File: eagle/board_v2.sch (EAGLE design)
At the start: 34 parts, among them J1 RJ11-4X, Q1 BD140, Q10 BD140, Q11 BD140, Q12 BD140, Q13 BD140, Q14 BD140, Q15 BD140, Q2 BD140, Q3 BD140, Q4 BD140, Q5 BD140, Q6 BD140, Q7 BD140, Q8 BD140, Q9 BD140, X1 RJ45-8X, X2 RJ45-8X, X3 RJ45-8X, X4 RJ45-8X, X5 RJ45-8X

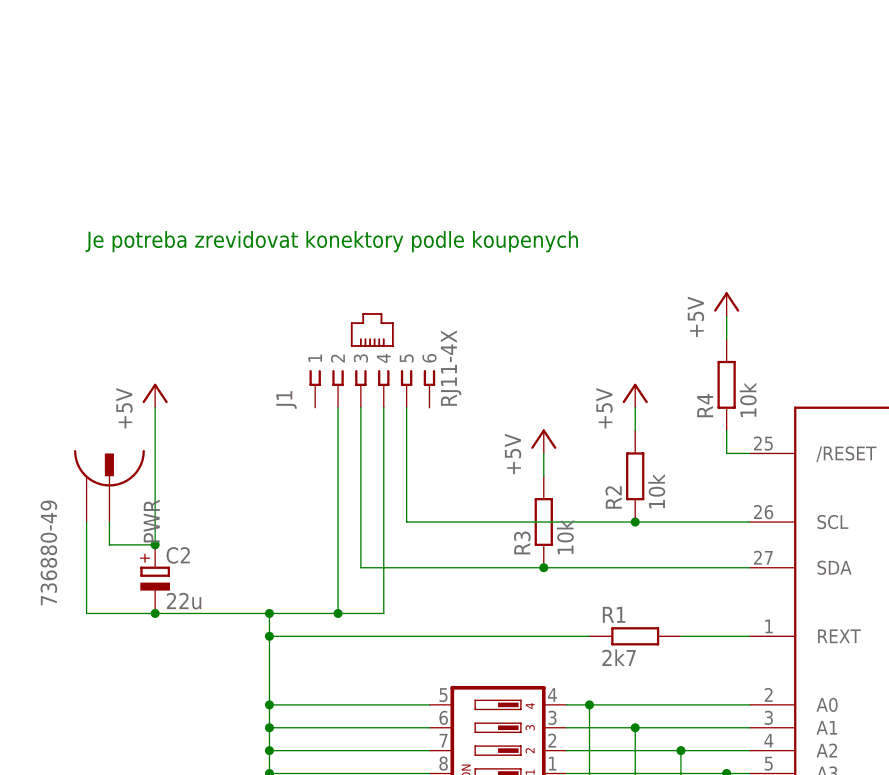
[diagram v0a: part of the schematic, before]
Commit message: board chaining connectors
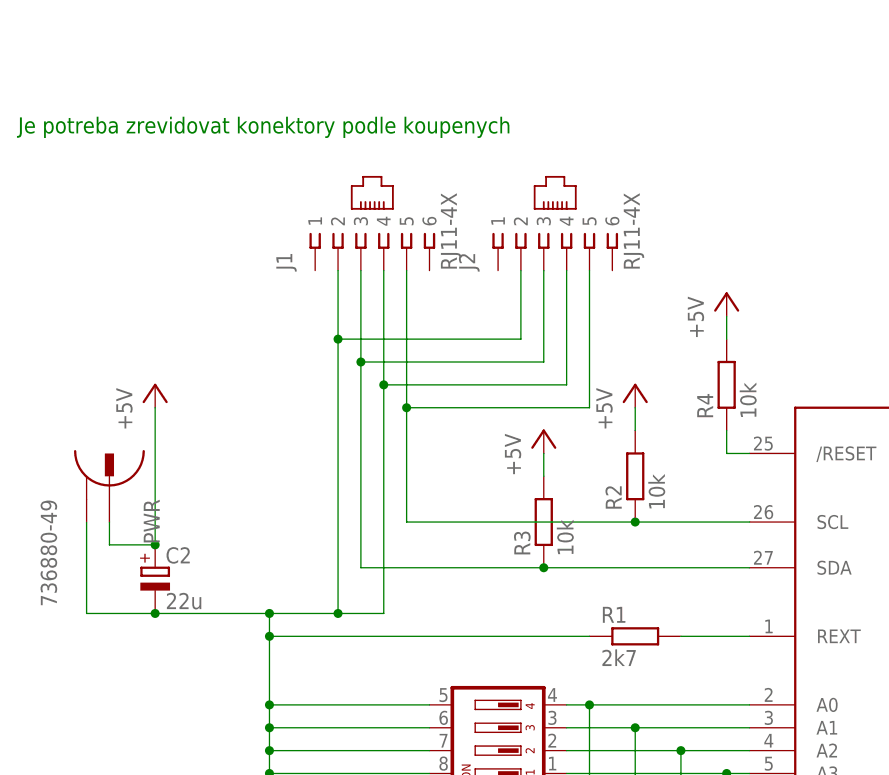
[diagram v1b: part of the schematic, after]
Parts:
- added J2: RJ11-4X, con-tycoelectronics:RJ11-4X
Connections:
- net GND: now also J2.2, J2.4
- net N$37: now also J2.5
- net N$38: now also J2.3
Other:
- moved on the sheet: J1
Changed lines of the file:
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@@
 <setting verticaltext="up"/>
 </settings>
-<grid distance="2.54" unitdist="mm" unit="mm" style="lines" multiple="1" display="yes" altdistance="0.254" altunitdist="mm" altunit="mm"/>
+<grid distance="0.1" unitdist="inch" unit="inch" style="lines" multiple="1" display="no" altdistance="0.01" altunitdist="inch" altunit="inch"/>
 <layers>
 <layer number="1" name="Top" color="4" fill="1" visible="no" active="no"/>
@@
 </part>
 <part name="J1" library="con-tycoelectronics" deviceset="RJ11" device="" technology="-4X"/>
+<part name="J2" library="con-tycoelectronics" deviceset="RJ11" device="" technology="-4X">
+<attribute name="MF" value=""/>
+<attribute name="MPN" value="6609214-3"/>
+<attribute name="OC_FARNELL" value="unknown"/>
+<attribute name="OC_NEWARK" value="19R7022"/>
+</part>
 </parts>
 <sheets>
 <sheet>
 <plain>
-<text x="-50.8" y="104.14" size="1.778" layer="91">Je potreba zrevidovat konektory podle koupenych</text>
+<text x="-58.42" y="116.84" size="1.778" layer="91">Je potreba zrevidovat konektory podle koupenych</text>
 </plain>
 <instances>
@@
 <instance part="P+11" gate="1" x="27.94" y="15.24" rot="R270"/>
 <instance part="S1" gate="A" x="-5.08" y="48.26" rot="R90"/>
-<instance part="J1" gate="G$1" x="-20.32" y="88.9" rot="R90"/>
+<instance part="J1" gate="G$1" x="-20.32" y="104.14" rot="R90"/>
+<instance part="J2" gate="G$1" x="0" y="104.14" rot="R90"/>
 </instances>
 <busses>
@@
 <junction x="-30.48" y="60.96"/>
 <pinref part="J1" gate="G$1" pin="4"/>
-<wire x1="-17.78" y1="63.5" x2="-17.78" y2="86.36" width="0.1524" layer="91"/>
+<wire x1="-17.78" y1="63.5" x2="-17.78" y2="88.9" width="0.1524" layer="91"/>
 <pinref part="J1" gate="G$1" pin="2"/>
-<wire x1="-22.86" y1="86.36" x2="-22.86" y2="63.5" width="0.1524" layer="91"/>
+<wire x1="-17.78" y1="88.9" x2="-17.78" y2="101.6" width="0.1524" layer="91"/>
+<wire x1="-22.86" y1="101.6" x2="-22.86" y2="93.98" width="0.1524" layer="91"/>
 <junction x="-22.86" y="63.5"/>
+<pinref part="J2" gate="G$1" pin="4"/>
+<wire x1="-22.86" y1="93.98" x2="-22.86" y2="63.5" width="0.1524" layer="91"/>
+<wire x1="2.54" y1="101.6" x2="2.54" y2="88.9" width="0.1524" layer="91"/>
+<wire x1="2.54" y1="88.9" x2="-17.78" y2="88.9" width="0.1524" layer="91"/>
+<pinref part="J2" gate="G$1" pin="2"/>
+<wire x1="-2.54" y1="101.6" x2="-2.54" y2="93.98" width="0.1524" layer="91"/>
+<wire x1="-2.54" y1="93.98" x2="-22.86" y2="93.98" width="0.1524" layer="91"/>
+<junction x="-17.78" y="88.9"/>
+<junction x="-22.86" y="93.98"/>
 </segment>
 <segment>
@@
 <pinref part="J1" gate="G$1" pin="5"/>
 <wire x1="-15.24" y1="73.66" x2="-15.24" y2="86.36" width="0.1524" layer="91"/>
+<pinref part="J2" gate="G$1" pin="5"/>
+<wire x1="-15.24" y1="86.36" x2="-15.24" y2="101.6" width="0.1524" layer="91"/>
+<wire x1="5.08" y1="101.6" x2="5.08" y2="86.36" width="0.1524" layer="91"/>
+<wire x1="5.08" y1="86.36" x2="-15.24" y2="86.36" width="0.1524" layer="91"/>
+<junction x="-15.24" y="86.36"/>
 </segment>
 </net>
@@
 <wire x1="22.86" y1="68.58" x2="0" y2="68.58" width="0.1524" layer="91"/>
 <pinref part="J1" gate="G$1" pin="3"/>
-<wire x1="-20.32" y1="86.36" x2="-20.32" y2="68.58" width="0.1524" layer="91"/>
+<wire x1="-20.32" y1="101.6" x2="-20.32" y2="91.44" width="0.1524" layer="91"/>
+<wire x1="-20.32" y1="91.44" x2="-20.32" y2="68.58" width="0.1524" layer="91"/>
 <wire x1="-20.32" y1="68.58" x2="0" y2="68.58" width="0.1524" layer="91"/>
 <junction x="0" y="68.58"/>
-</segment>
-</net>
+<pinref part="J2" gate="G$1" pin="3"/>
+<wire x1="0" y1="101.6" x2="0" y2="91.44" width="0.1524" layer="91"/>
+<wire x1="0" y1="91.44" x2="-20.32" y2="91.44" width="0.1524" layer="91"/>
+<junction x="-20.32" y="91.44"/>
+</segment>
+</net>

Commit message: cinch -> svorkovnice
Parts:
- removed PWR: 736880-49, con-conrad:736880-49
- added GND, VCC: WIREPAD3,17/1,3, wirepad:WIREPAD3,17/1,3
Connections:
- net +5V: now also VCC.P; no longer PWR.1
- net GND: now also GND.P; no longer PWR.2
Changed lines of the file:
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@@
 <part name="U$1" library="tlc" deviceset="TLC59116" device=""/>
 <part name="GND9" library="supply1" deviceset="GND" device=""/>
-<part name="PWR" library="con-conrad" deviceset="736880-49" device=""/>
 <part name="P+7" library="supply1" deviceset="+5V" device=""/>
 <part name="P+8" library="supply1" deviceset="+5V" device=""/>
@@
 <attribute name="OC_NEWARK" value="19R7022"/>
 </part>
+<part name="GND" library="wirepad" deviceset="WIREPAD" device="3,17/1,3"/>
+<part name="VCC" library="wirepad" deviceset="WIREPAD" device="3,17/1,3"/>
 </parts>
 <sheets>
@@
 <instance part="U$1" gate="G$1" x="48.26" y="63.5"/>
 <instance part="GND9" gate="1" x="-30.48" y="40.64"/>
-<instance part="PWR" gate="G$1" x="-48.26" y="76.2" rot="R270"/>
 <instance part="P+7" gate="1" x="10.16" y="88.9"/>
 <instance part="P+8" gate="1" x="0" y="83.82"/>
@@
 <instance part="J1" gate="G$1" x="-20.32" y="104.14" rot="R90"/>
 <instance part="J2" gate="G$1" x="0" y="104.14" rot="R90"/>
+<instance part="GND" gate="G$1" x="-68.58" y="91.44" rot="R270"/>
+<instance part="VCC" gate="G$1" x="-58.42" y="91.44" rot="R270"/>
 </instances>
 <busses>
@@
 <pinref part="C2" gate="G$1" pin="+"/>
 <wire x1="-43.18" y1="86.36" x2="-43.18" y2="71.12" width="0.1524" layer="91"/>
-<pinref part="PWR" gate="G$1" pin="1"/>
-<wire x1="-48.26" y1="73.66" x2="-48.26" y2="71.12" width="0.1524" layer="91"/>
-<wire x1="-43.18" y1="71.12" x2="-48.26" y2="71.12" width="0.1524" layer="91"/>
 <junction x="-43.18" y="71.12"/>
+<pinref part="VCC" gate="G$1" pin="P"/>
+<wire x1="-43.18" y1="71.12" x2="-58.42" y2="71.12" width="0.1524" layer="91"/>
+<wire x1="-58.42" y1="71.12" x2="-58.42" y2="88.9" width="0.1524" layer="91"/>
 </segment>
 <segment>
@@
 <pinref part="S1" gate="A" pin="7"/>
 <pinref part="S1" gate="A" pin="8"/>
-<pinref part="PWR" gate="G$1" pin="2"/>
-<wire x1="-50.8" y1="73.66" x2="-50.8" y2="63.5" width="0.1524" layer="91"/>
-<wire x1="-50.8" y1="63.5" x2="-43.18" y2="63.5" width="0.1524" layer="91"/>
+<wire x1="-68.58" y1="88.9" x2="-68.58" y2="63.5" width="0.1524" layer="91"/>
+<wire x1="-68.58" y1="63.5" x2="-43.18" y2="63.5" width="0.1524" layer="91"/>
 <wire x1="-43.18" y1="63.5" x2="-30.48" y2="63.5" width="0.1524" layer="91"/>
 <wire x1="-30.48" y1="63.5" x2="-22.86" y2="63.5" width="0.1524" layer="91"/>
@@
 <junction x="-17.78" y="88.9"/>
 <junction x="-22.86" y="93.98"/>
-</segment>
-<segment>
+<pinref part="GND" gate="G$1" pin="P"/>
+</segment>
+<segment>

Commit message: moar changes
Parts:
- removed GND, VCC: WIREPAD3,17/1,3, wirepad:WIREPAD3,17/1,3
- added X6: RJ45-8X, con-tycoelectronics:RJ45-8X
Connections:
- net +5V: now also X6.1, X6.2, X6.3, X6.4; no longer VCC.P
- net GND: now also X6.5, X6.6, X6.7, X6.8; no longer GND.P
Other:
- note removed: "Je potreba zrevidovat konektory podle koupenych"
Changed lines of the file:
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@@
 <attribute name="OC_NEWARK" value="19R7022"/>
 </part>
-<part name="GND" library="wirepad" deviceset="WIREPAD" device="3,17/1,3"/>
-<part name="VCC" library="wirepad" deviceset="WIREPAD" device="3,17/1,3"/>
+<part name="X6" library="con-tycoelectronics" deviceset="RJ45" device="" technology="-8X"/>
 </parts>
 <sheets>
 <sheet>
 <plain>
-<text x="-58.42" y="116.84" size="1.778" layer="91">Je potreba zrevidovat konektory podle koupenych</text>
 </plain>
 <instances>
@@
 <instance part="J1" gate="G$1" x="-20.32" y="104.14" rot="R90"/>
 <instance part="J2" gate="G$1" x="0" y="104.14" rot="R90"/>
-<instance part="GND" gate="G$1" x="-68.58" y="91.44" rot="R270"/>
-<instance part="VCC" gate="G$1" x="-58.42" y="91.44" rot="R270"/>
+<instance part="X6" gate="G$1" x="-63.5" y="106.68" rot="MR90"/>
 </instances>
 <busses>
@@
 <wire x1="-43.18" y1="86.36" x2="-43.18" y2="71.12" width="0.1524" layer="91"/>
 <junction x="-43.18" y="71.12"/>
-<pinref part="VCC" gate="G$1" pin="P"/>
 <wire x1="-43.18" y1="71.12" x2="-58.42" y2="71.12" width="0.1524" layer="91"/>
-<wire x1="-58.42" y1="71.12" x2="-58.42" y2="88.9" width="0.1524" layer="91"/>
+<wire x1="-58.42" y1="71.12" x2="-58.42" y2="101.6" width="0.1524" layer="91"/>
+<wire x1="-58.42" y1="101.6" x2="-55.88" y2="101.6" width="0.1524" layer="91"/>
+<pinref part="X6" gate="G$1" pin="1"/>
+<wire x1="-55.88" y1="101.6" x2="-55.88" y2="104.14" width="0.1524" layer="91"/>
+<pinref part="X6" gate="G$1" pin="2"/>
+<wire x1="-58.42" y1="101.6" x2="-58.42" y2="104.14" width="0.1524" layer="91"/>
+<pinref part="X6" gate="G$1" pin="3"/>
+<wire x1="-58.42" y1="101.6" x2="-60.96" y2="101.6" width="0.1524" layer="91"/>
+<wire x1="-60.96" y1="101.6" x2="-60.96" y2="104.14" width="0.1524" layer="91"/>
+<pinref part="X6" gate="G$1" pin="4"/>
+<wire x1="-60.96" y1="101.6" x2="-63.5" y2="101.6" width="0.1524" layer="91"/>
+<wire x1="-63.5" y1="101.6" x2="-63.5" y2="104.14" width="0.1524" layer="91"/>
+<junction x="-58.42" y="101.6"/>
 </segment>
 <segment>
@@
 <pinref part="S1" gate="A" pin="7"/>
 <pinref part="S1" gate="A" pin="8"/>
-<wire x1="-68.58" y1="88.9" x2="-68.58" y2="63.5" width="0.1524" layer="91"/>
+<wire x1="-68.58" y1="104.14" x2="-68.58" y2="101.6" width="0.1524" layer="91"/>
+<wire x1="-68.58" y1="101.6" x2="-68.58" y2="63.5" width="0.1524" layer="91"/>
 <wire x1="-68.58" y1="63.5" x2="-43.18" y2="63.5" width="0.1524" layer="91"/>
 <wire x1="-43.18" y1="63.5" x2="-30.48" y2="63.5" width="0.1524" layer="91"/>
@@
 <junction x="-17.78" y="88.9"/>
 <junction x="-22.86" y="93.98"/>
-<pinref part="GND" gate="G$1" pin="P"/>
-</segment>
-<segment>
+<pinref part="X6" gate="G$1" pin="6"/>
+<pinref part="X6" gate="G$1" pin="8"/>
+<wire x1="-68.58" y1="101.6" x2="-71.12" y2="101.6" width="0.1524" layer="91"/>
+<wire x1="-71.12" y1="101.6" x2="-73.66" y2="101.6" width="0.1524" layer="91"/>
+<wire x1="-73.66" y1="101.6" x2="-73.66" y2="104.14" width="0.1524" layer="91"/>
+<pinref part="X6" gate="G$1" pin="7"/>
+<wire x1="-71.12" y1="101.6" x2="-71.12" y2="104.14" width="0.1524" layer="91"/>
+<pinref part="X6" gate="G$1" pin="5"/>
+<wire x1="-68.58" y1="101.6" x2="-66.04" y2="101.6" width="0.1524" layer="91"/>
+<wire x1="-66.04" y1="101.6" x2="-66.04" y2="104.14" width="0.1524" layer="91"/>
+<junction x="-68.58" y="101.6"/>
+</segment>
+<segment>

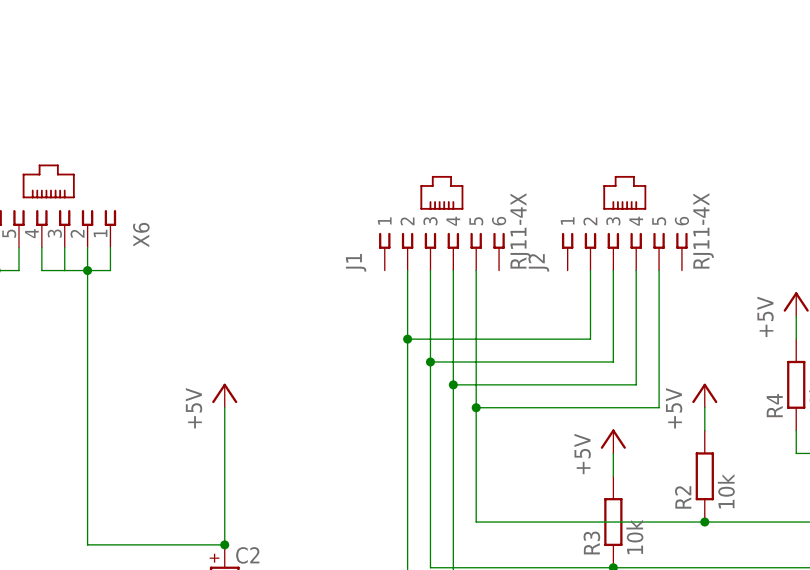
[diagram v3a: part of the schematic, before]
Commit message: i2c in crossover; removed jumper wires
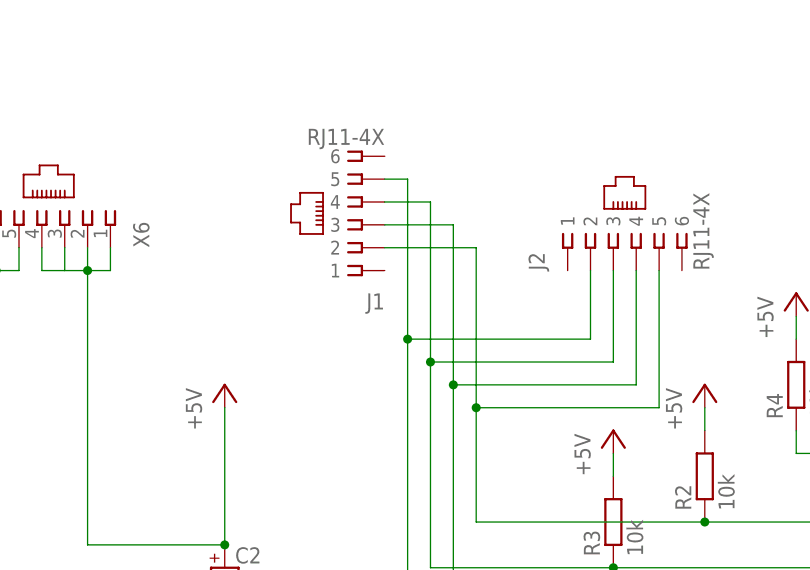
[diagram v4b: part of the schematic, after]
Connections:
- net GND: now also J1.3, J1.5; no longer J1.2, J1.4
- net N$37: now also J1.2; no longer J1.5
- net N$38: now also J1.4; no longer J1.3
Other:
- moved on the sheet: J1
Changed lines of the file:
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@@
 <instance part="P+11" gate="1" x="27.94" y="15.24" rot="R270"/>
 <instance part="S1" gate="A" x="-5.08" y="48.26" rot="R90"/>
-<instance part="J1" gate="G$1" x="-20.32" y="104.14" rot="R90"/>
+<instance part="J1" gate="G$1" x="-27.94" y="106.68" rot="R180"/>
 <instance part="J2" gate="G$1" x="0" y="104.14" rot="R90"/>
 <instance part="X6" gate="G$1" x="-63.5" y="106.68" rot="MR90"/>
@@
 <junction x="-30.48" y="63.5"/>
 <junction x="-30.48" y="60.96"/>
-<pinref part="J1" gate="G$1" pin="4"/>
 <wire x1="-17.78" y1="63.5" x2="-17.78" y2="88.9" width="0.1524" layer="91"/>
-<pinref part="J1" gate="G$1" pin="2"/>
-<wire x1="-17.78" y1="88.9" x2="-17.78" y2="101.6" width="0.1524" layer="91"/>
-<wire x1="-22.86" y1="101.6" x2="-22.86" y2="93.98" width="0.1524" layer="91"/>
 <junction x="-22.86" y="63.5"/>
 <pinref part="J2" gate="G$1" pin="4"/>
@@
 <wire x1="-2.54" y1="101.6" x2="-2.54" y2="93.98" width="0.1524" layer="91"/>
 <wire x1="-2.54" y1="93.98" x2="-22.86" y2="93.98" width="0.1524" layer="91"/>
-<junction x="-17.78" y="88.9"/>
-<junction x="-22.86" y="93.98"/>
 <pinref part="X6" gate="G$1" pin="6"/>
 <pinref part="X6" gate="G$1" pin="8"/>
@@
 <wire x1="-66.04" y1="101.6" x2="-66.04" y2="104.14" width="0.1524" layer="91"/>
 <junction x="-68.58" y="101.6"/>
+<pinref part="J1" gate="G$1" pin="3"/>
+<wire x1="-25.4" y1="106.68" x2="-17.78" y2="106.68" width="0.1524" layer="91"/>
+<wire x1="-17.78" y1="106.68" x2="-17.78" y2="88.9" width="0.1524" layer="91"/>
+<pinref part="J1" gate="G$1" pin="5"/>
+<wire x1="-25.4" y1="111.76" x2="-22.86" y2="111.76" width="0.1524" layer="91"/>
+<wire x1="-22.86" y1="111.76" x2="-22.86" y2="93.98" width="0.1524" layer="91"/>
+<junction x="-22.86" y="93.98"/>
+<junction x="-17.78" y="88.9"/>
 </segment>
 <segment>
@@
 <wire x1="10.16" y1="73.66" x2="-15.24" y2="73.66" width="0.1524" layer="91"/>
 <junction x="10.16" y="73.66"/>
-<pinref part="J1" gate="G$1" pin="5"/>
 <wire x1="-15.24" y1="73.66" x2="-15.24" y2="86.36" width="0.1524" layer="91"/>
 <pinref part="J2" gate="G$1" pin="5"/>
-<wire x1="-15.24" y1="86.36" x2="-15.24" y2="101.6" width="0.1524" layer="91"/>
 <wire x1="5.08" y1="101.6" x2="5.08" y2="86.36" width="0.1524" layer="91"/>
 <wire x1="5.08" y1="86.36" x2="-15.24" y2="86.36" width="0.1524" layer="91"/>
+<pinref part="J1" gate="G$1" pin="2"/>
+<wire x1="-25.4" y1="104.14" x2="-15.24" y2="104.14" width="0.1524" layer="91"/>
+<wire x1="-15.24" y1="104.14" x2="-15.24" y2="86.36" width="0.1524" layer="91"/>
 <junction x="-15.24" y="86.36"/>
 </segment>
@@
 <pinref part="R3" gate="G$1" pin="1"/>
 <wire x1="22.86" y1="68.58" x2="0" y2="68.58" width="0.1524" layer="91"/>
-<pinref part="J1" gate="G$1" pin="3"/>
-<wire x1="-20.32" y1="101.6" x2="-20.32" y2="91.44" width="0.1524" layer="91"/>
 <wire x1="-20.32" y1="91.44" x2="-20.32" y2="68.58" width="0.1524" layer="91"/>
 <wire x1="-20.32" y1="68.58" x2="0" y2="68.58" width="0.1524" layer="91"/>
@@
 <wire x1="0" y1="101.6" x2="0" y2="91.44" width="0.1524" layer="91"/>
 <wire x1="0" y1="91.44" x2="-20.32" y2="91.44" width="0.1524" layer="91"/>
+<pinref part="J1" gate="G$1" pin="4"/>
+<wire x1="-25.4" y1="109.22" x2="-20.32" y2="109.22" width="0.1524" layer="91"/>
+<wire x1="-20.32" y1="109.22" x2="-20.32" y2="91.44" width="0.1524" layer="91"/>
 <junction x="-20.32" y="91.44"/>
 </segment>

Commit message: board v2.2
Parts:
- removed S1: (no value), switch-dil:DS04
- removed X1, X2, X3, X4, X5: RJ45-8X, con-tycoelectronics:RJ45-8X
- added C3: 1u, resistor:C-EUC1206
- added JP1: (no value), pinhead:PINHD-2X4
- added PWR: ARK210/2EX, con-brm:ARK210/2EX
- added X10, X7, X8, X9: 22-23-2041, con-molex:22-23-2041
- C2: device resistor:CPOL-EUC -> resistor:CPOL-EUE2.5-5
- R4: value 10k -> 4k7
- X6: value RJ45-8X -> 22-23-2041; device con-tycoelectronics:RJ45-8X -> con-molex:22-23-2041
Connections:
- net +5V: now also C3.1, PWR.1, X10-2.S, X6-2.S, X7-2.S, X8-2.S, X9-2.S; no longer X1.4, X2.4, X3.4, X4.4, X5.4, X6.1, X6.2, X6.3, X6.4
- net GND: now also C3.2, JP1.1, JP1.3, JP1.5, JP1.7, PWR.2; no longer S1.5, S1.6, S1.7, S1.8, X6.5, X6.6, X6.7, X6.8
- net N$1: now also X6-1.S; no longer X1.2
- net N$10: now also X10-1.S; no longer X4.2
- net N$11: now also X10-3.S; no longer X4.6
- net N$12: now also X10-4.S; no longer X4.8
- net N$13: now also X7-1.S; no longer X5.2
- net N$14: now also X7-3.S; no longer X5.6
- net N$15: now also X7-4.S; no longer X5.8
- net N$17: now also JP1.2; no longer S1.4
- net N$18: now also JP1.4; no longer S1.3
- net N$19: now also JP1.6; no longer S1.2
- net N$2: now also X6-3.S; no longer X1.6
- net N$20: now also JP1.8; no longer S1.1
- net N$3: now also X6-4.S; no longer X1.8
- net N$4: now also X8-1.S; no longer X2.2
- net N$5: now also X8-3.S; no longer X2.6
- net N$6: now also X8-4.S; no longer X2.8
- net N$7: now also X9-1.S; no longer X3.2
- net N$8: now also X9-3.S; no longer X3.6
- net N$9: now also X9-4.S; no longer X3.8
